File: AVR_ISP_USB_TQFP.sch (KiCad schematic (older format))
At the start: 19 parts, among them IC1 ATMEGA8-AI, J1 USB, P1 CONN_02X05, X1 CRYSTAL

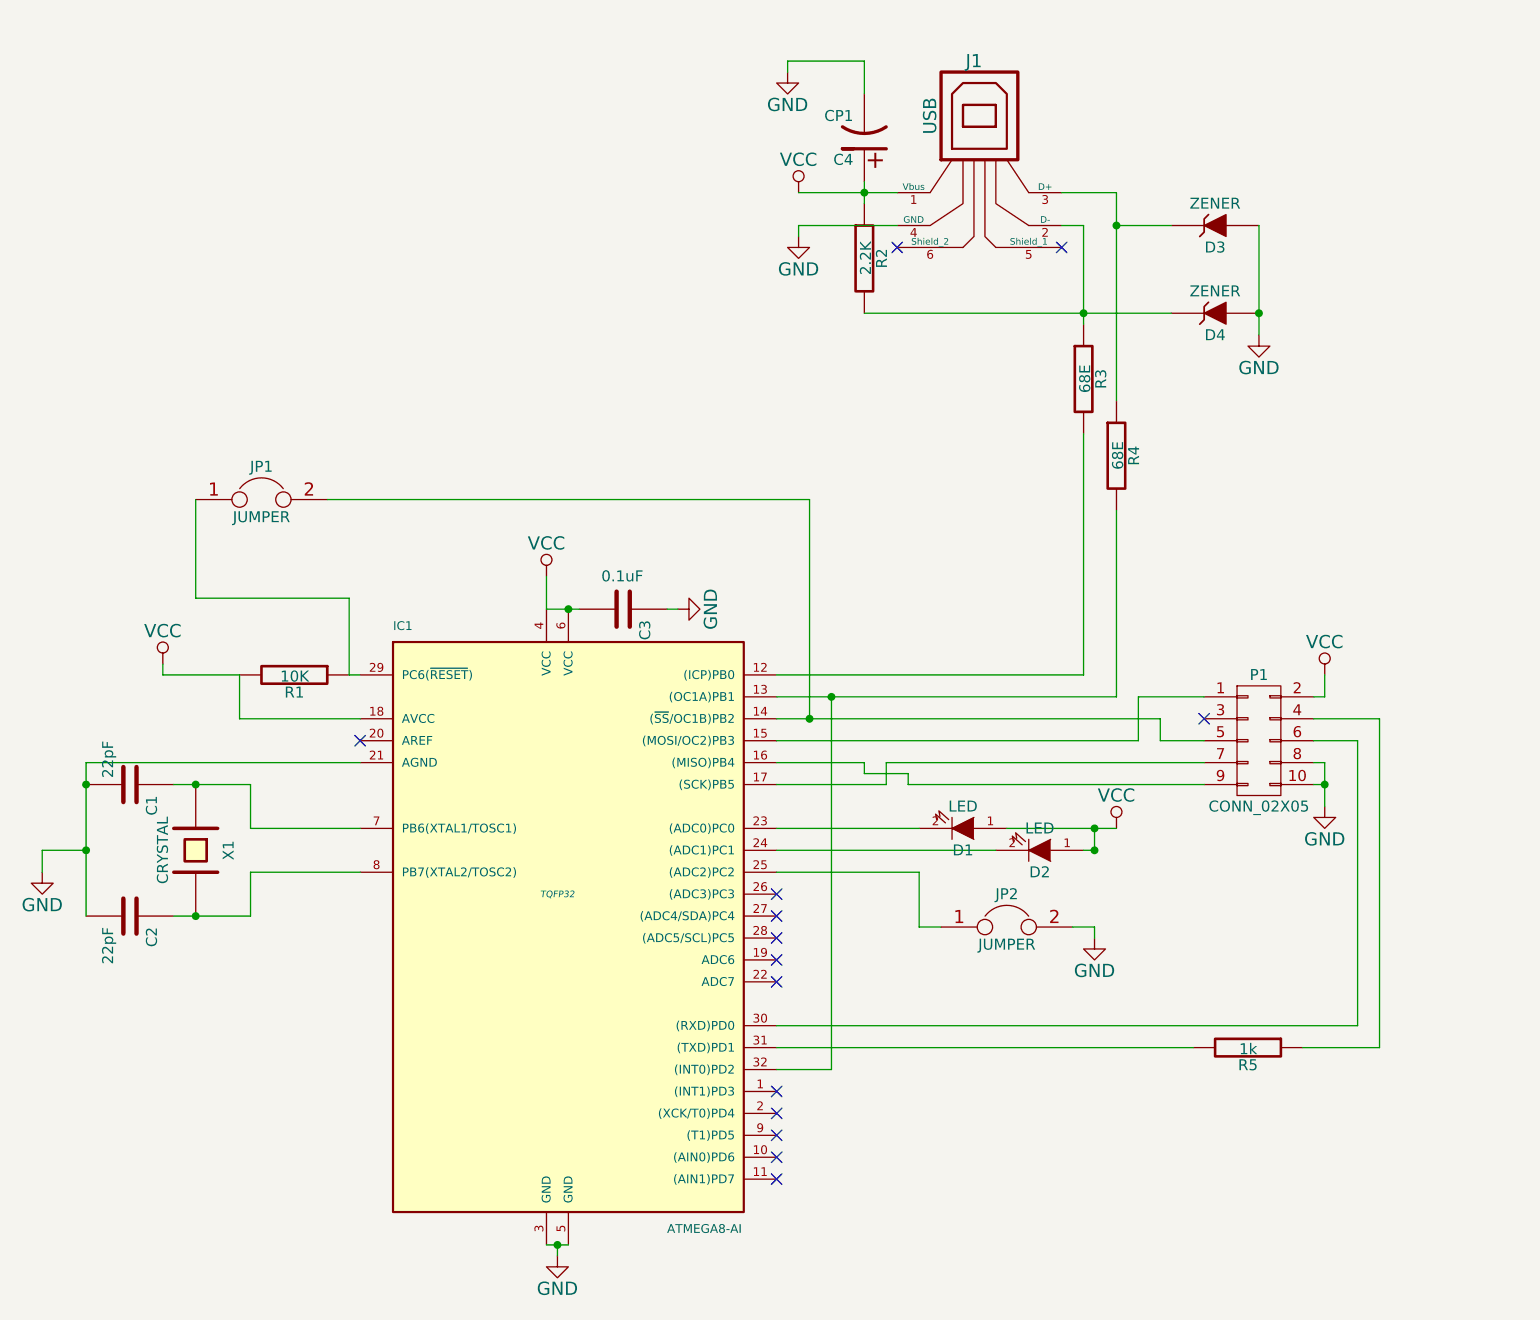
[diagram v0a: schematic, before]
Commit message: added complete layout
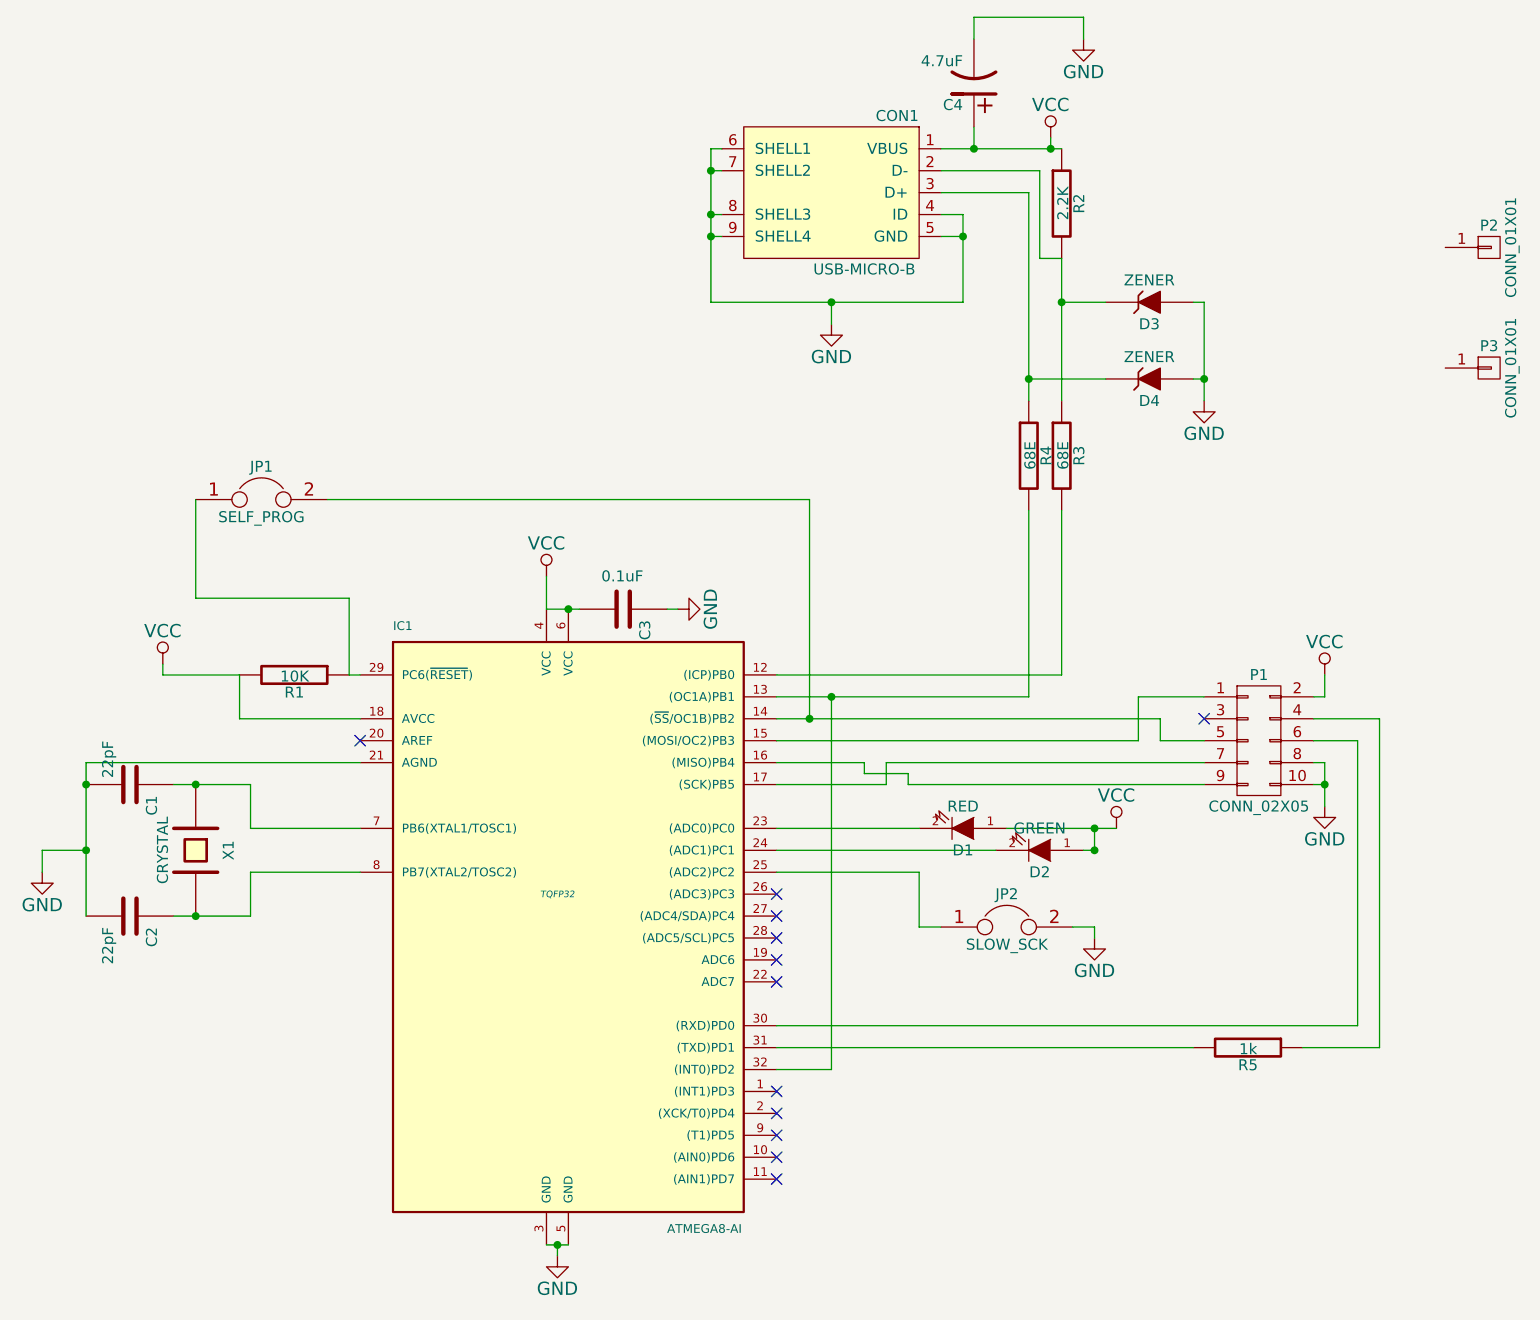
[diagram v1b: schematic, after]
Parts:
- removed J1: USB, symbol USB
- added CON1: USB-MICRO-B, symbol USB-MICRO-B
- added P2, P3: CONN_01X01, symbol CONN_01X01
- C4: value CP1 -> 4.7uF
- D1: value LED -> RED
- D2: value LED -> GREEN
- JP1: value JUMPER -> SELF_PROG
- JP2: value JUMPER -> SLOW_SCK
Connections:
- net GND: now also CON1.4 (ID), CON1.5 (GND), CON1.6 (SHELL1), CON1.7 (SHELL2), CON1.8 (SHELL3), CON1.9 (SHELL4)
- net VCC: now also CON1.1 (VBUS)
- net at R2.2, R3.1: now also D3.2 (K), CON1.2 (D-); no longer D4.2 (K)
- net at R4.1: now also D4.2 (K), CON1.3 (D+); no longer D3.2 (K)
- no-connect marks 14 -> 12
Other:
- moved on the sheet: C4, D3, D4, R2, R3, R4

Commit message: final
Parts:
- added P4, P5: CONN_01X01, symbol CONN_01X01
- added R6, R7: 1k, symbol R
- D3, D4: value ZENER -> 3.6V
- X1: value CRYSTAL -> 12MHz
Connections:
- net VCC: now also R6.1, R7.1; no longer D1.1 (A), D2.1 (A)
- new net: D1.1 (A), R6.2
- new net: D2.1 (A), R7.2
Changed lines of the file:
@@
 P 3800 4300
 F 0 "X1" H 3800 4450 50  0000 C CNN
-F 1 "CRYSTAL" H 3800 4150 50  0000 C CNN
+F 1 "12MHz" H 3800 4150 50  0000 C CNN
 F 2 "" H 3800 4300 60  0000 C CNN
 F 3 "" H 3800 4300 60  0000 C CNN
@@
 $EndComp
 $Comp
-L GND #PWR01
+L GND #PWR1
 U 1 1 55F26B7A
 P 3100 4400
-F 0 "#PWR01" H 3100 4150 60  0001 C CNN
+F 0 "#PWR1" H 3100 4150 60  0001 C CNN
 F 1 "GND" H 3100 4250 60  0000 C CNN
 F 2 "" H 3100 4400 60  0000 C CNN
@@
 $EndComp
 $Comp
-L VCC #PWR02
+L VCC #PWR2
 U 1 1 55F26D16
 P 3650 3450
-F 0 "#PWR02" H 3650 3300 60  0001 C CNN
+F 0 "#PWR2" H 3650 3300 60  0001 C CNN
 F 1 "VCC" H 3650 3600 60  0000 C CNN
 F 2 "" H 3650 3450 60  0000 C CNN
@@
 $EndComp
 $Comp
-L VCC #PWR03
+L VCC #PWR3
 U 1 1 55F26D63
 P 5400 3050
-F 0 "#PWR03" H 5400 2900 60  0001 C CNN
+F 0 "#PWR3" H 5400 2900 60  0001 C CNN
 F 1 "VCC" H 5400 3200 60  0000 C CNN
 F 2 "" H 5400 3050 60  0000 C CNN
@@
 $EndComp
 $Comp
-L GND #PWR04
+L GND #PWR5
 U 1 1 55F26E60
 P 6000 3200
-F 0 "#PWR04" H 6000 2950 60  0001 C CNN
+F 0 "#PWR5" H 6000 2950 60  0001 C CNN
 F 1 "GND" H 6000 3050 60  0000 C CNN
 F 2 "" H 6000 3200 60  0000 C CNN
@@
 $EndComp
 $Comp
-L GND #PWR05
+L GND #PWR8
 U 1 1 55F2753B
 P 7850 600
-F 0 "#PWR05" H 7850 350 60  0001 C CNN
+F 0 "#PWR8" H 7850 350 60  0001 C CNN
 F 1 "GND" H 7850 450 60  0000 C CNN
 F 2 "" H 7850 600 60  0000 C CNN
@@
 P 8150 1800
 F 0 "D3" H 8150 1900 50  0000 C CNN
-F 1 "ZENER" H 8150 1700 50  0000 C CNN
+F 1 "3.6V" H 8150 1700 50  0000 C CNN
 F 2 "" H 8150 1800 60  0000 C CNN
 F 3 "" H 8150 1800 60  0000 C CNN
@@
 P 8150 2150
 F 0 "D4" H 8150 2250 50  0000 C CNN
-F 1 "ZENER" H 8150 2050 50  0000 C CNN
+F 1 "3.6V" H 8150 2050 50  0000 C CNN
 F 2 "" H 8150 2150 60  0000 C CNN
 F 3 "" H 8150 2150 60  0000 C CNN
@@
 $EndComp
 $Comp
-L GND #PWR06
+L GND #PWR6
 U 1 1 55F28493
 P 6700 1900
-F 0 "#PWR06" H 6700 1650 60  0001 C CNN
+F 0 "#PWR6" H 6700 1650 60  0001 C CNN
 F 1 "GND" H 6700 1750 60  0000 C CNN
 F 2 "" H 6700 1900 60  0000 C CNN
@@
 	6850 3900 6450 3900
 $Comp
-L VCC #PWR07
+L VCC #PWR12
 U 1 1 55F2914B
 P 8950 3500
-F 0 "#PWR07" H 8950 3350 60  0001 C CNN
+F 0 "#PWR12" H 8950 3350 60  0001 C CNN
 F 1 "VCC" H 8950 3650 60  0000 C CNN
 F 2 "" H 8950 3500 60  0000 C CNN
@@
 	8950 4000 8900 4000
 $Comp
-L GND #PWR08
+L GND #PWR13
 U 1 1 55F299EF
 P 8950 4100
-F 0 "#PWR08" H 8950 3850 60  0001 C CNN
+F 0 "#PWR13" H 8950 3850 60  0001 C CNN
 F 1 "GND" H 8950 3950 60  0000 C CNN
 F 2 "" H 8950 4100 60  0000 C CNN
@@
 Wire Wire Line
 	6450 4300 7450 4300
-Wire Wire Line
-	7500 4200 8000 4200
-Wire Wire Line
-	7900 4300 7850 4300
-Connection ~ 7900 4300
-$Comp
-L VCC #PWR09
+$Comp
+L VCC #PWR10
 U 1 1 55F29FF6
-P 8000 4200
-F 0 "#PWR09" H 8000 4050 60  0001 C CNN
-F 1 "VCC" H 8000 4350 60  0000 C CNN
-F 2 "" H 8000 4200 60  0000 C CNN
-F 3 "" H 8000 4200 60  0000 C CNN
-	1    8000 4200
-	1    0    0    -1
-$EndComp
-Wire Wire Line
-	7900 4200 7900 4300
-Connection ~ 7900 4200
+P 8300 4150
+F 0 "#PWR10" H 8300 4000 60  0001 C CNN
+F 1 "VCC" H 8300 4300 60  0000 C CNN
+F 2 "" H 8300 4150 60  0000 C CNN
+F 3 "" H 8300 4150 60  0000 C CNN
+	1    8300 4150
+	1    0    0    -1
+$EndComp
 $Comp
 L JUMPER JP2
@@
 	7100 4650 7200 4650
 $Comp
-L GND #PWR010
+L GND #PWR9
 U 1 1 55F2A439
 P 7900 4700
-F 0 "#PWR010" H 7900 4450 60  0001 C CNN
+F 0 "#PWR9" H 7900 4450 60  0001 C CNN
 F 1 "GND" H 7900 4550 60  0000 C CNN
 F 2 "" H 7900 4700 60  0000 C CNN
@@
 	5400 6100 5500 6100
 $Comp
-L GND #PWR011
+L GND #PWR4
 U 1 1 55F2A778
 P 5450 6150
-F 0 "#PWR011" H 5450 5900 60  0001 C CNN
+F 0 "#PWR4" H 5450 5900 60  0001 C CNN
 F 1 "GND" H 5450 6000 60  0000 C CNN
 F 2 "" H 5450 6150 60  0000 C CNN
@@
 	7850 500  7850 600
 $Comp
-L VCC #PWR012
+L VCC #PWR7
 U 1 1 55FCFE9A
 P 7700 1050
-F 0 "#PWR012" H 7700 900 60  0001 C CNN
+F 0 "#PWR7" H 7700 900 60  0001 C CNN
 F 1 "VCC" H 7700 1200 60  0000 C CNN
 F 2 "" H 7700 1050 60  0000 C CNN
@@
 	8400 2150 8350 2150
 $Comp
-L GND #PWR013
+L GND #PWR11
 U 1 1 55FD0D6A
 P 8400 2250
-F 0 "#PWR013" H 8400 2000 60  0001 C CNN
+F 0 "#PWR11" H 8400 2000 60  0001 C CNN
 F 1 "GND" H 8400 2100 60  0000 C CNN
 F 2 "" H 8400 2250 60  0000 C CNN
@@
 	1    0    0    -1
 $EndComp
+$Comp
+L CONN_01X01 P4
+U 1 1 56016B19
+P 9700 2650
+F 0 "P4" H 9700 2750 50  0000 C CNN
+F 1 "CONN_01X01" V 9800 2650 50  0000 C CNN
+F 2 "" H 9700 2650 60  0000 C CNN
+F 3 "" H 9700 2650 60  0000 C CNN
+	1    9700 2650
+	1    0    0    -1
+$EndComp
+$Comp
+L CONN_01X01 P5
+U 1 1 56016B53
+P 9700 3200
+F 0 "P5" H 9700 3300 50  0000 C CNN
+F 1 "CONN_01X01" V 9800 3200 50  0000 C CNN
+F 2 "" H 9700 3200 60  0000 C CNN
+F 3 "" H 9700 3200 60  0000 C CNN
+	1    9700 3200
+	1    0    0    -1
+$EndComp
+$Comp
+L R R6
+U 1 1 56022BE0
+P 7850 4200
+F 0 "R6" V 7930 4200 50  0000 C CNN
+F 1 "1k" V 7857 4201 50  0000 C CNN
+F 2 "" V 7780 4200 30  0000 C CNN
+F 3 "" H 7850 4200 30  0000 C CNN
+	1    7850 4200
+	0    1    1    0
+$EndComp
+$Comp
+L R R7
+U 1 1 56022C94
+P 8150 4300
+F 0 "R7" V 8230 4300 50  0000 C CNN
+F 1 "1k" V 8157 4301 50  0000 C CNN
+F 2 "" V 8080 4300 30  0000 C CNN
+F 3 "" H 8150 4300 30  0000 C CNN
+	1    8150 4300
+	0    1    1    0
+$EndComp
+Wire Wire Line
+	7500 4200 7600 4200
+Wire Wire Line
+	7850 4300 7900 4300
+Wire Wire Line
+	8400 4300 8400 4200
+Wire Wire Line
+	8400 4200 8100 4200
+Wire Wire Line
+	8300 4150 8300 4200
+Connection ~ 8300 4200
 $EndSCHEMATC
